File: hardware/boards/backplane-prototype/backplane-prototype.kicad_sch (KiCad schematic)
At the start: 32 parts, among them J1 DC_IN, J2 SLOT_1, J3 SLOT_2, J4 SLOT_3, J5 SLOT_4, J6 SLOT_5, J7 SLOT_6, J8 i2c_busses

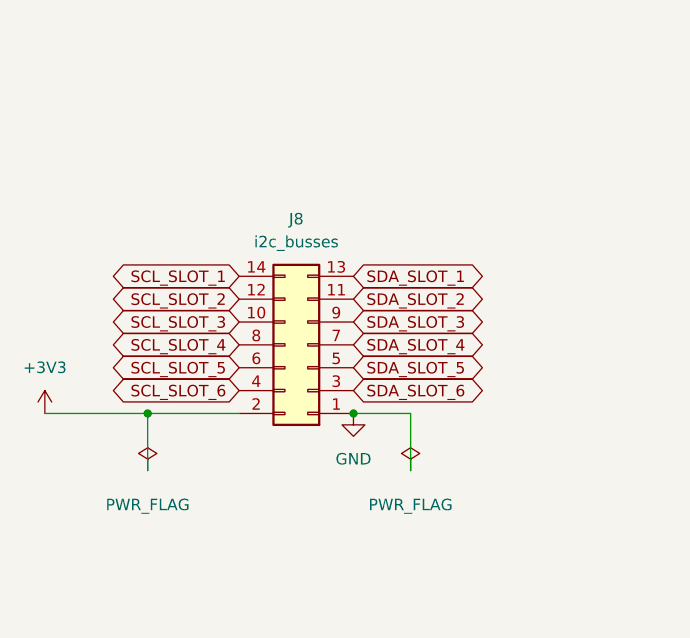
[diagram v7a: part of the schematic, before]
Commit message: feat: connect slot power controls
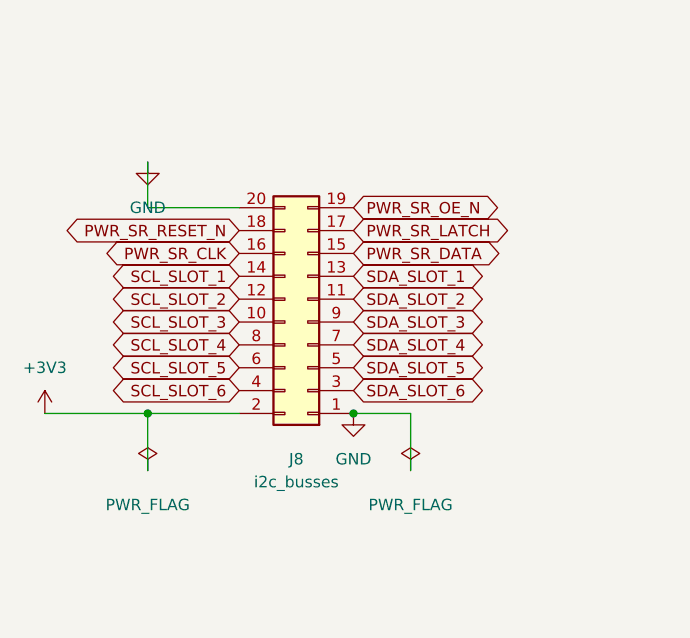
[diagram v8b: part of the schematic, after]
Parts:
- J8: footprint Connector_PinHeader_1.00mm:PinHeader_2x07_P1.00mm_Vertical -> Connector_PinHeader_1.00mm:PinHeader_2x10_P1.00mm_Vertical; symbol Connector_Generic:Conn_02x07_Odd_Even -> Connector_Generic:Conn_02x10_Odd_Even
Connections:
- net GND: now also J8.20 (Pin_20)
- new net PWR_SR_CLK: J8.16 (Pin_16)
- new net PWR_SR_DATA: J8.15 (Pin_15)
- new net PWR_SR_LATCH: J8.17 (Pin_17)
- new net PWR_SR_OE_N: J8.19 (Pin_19)
- new net PWR_SR_RESET_N: J8.18 (Pin_18)
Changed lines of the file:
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@@
 		)
 	)
+	(wire
+		(pts
+			(xy 41.91 140.97) (xy 31.75 140.97)
+		)
+		(stroke
+			(width 0)
+			(type default)
+		)
+	)
+	(wire
+		(pts
+			(xy 31.75 140.97) (xy 31.75 135.89)
+		)
+		(stroke
+			(width 0)
+			(type default)
+		)
+	)
 	(global_label "GND"
 		(shape bidirectional)
@@
 		)
 	)
+	(global_label "PWR_SR_DATA"
+		(shape bidirectional)
+		(at 54.61 146.05 0)
+		(effects
+			(font
+				(size 1.27 1.27)
+			)
+			(justify left)
+		)
+		(property "Intersheetrefs" "${INTERSHEET_REFS}"
+			(at 54.61 146.05 0)
+			(hide yes)
+			(show_name no)
+			(do_not_autoplace no)
+			(effects
+				(font
+					(size 1.27 1.27)
+				)
+			)
+		)
+	)
+	(global_label "PWR_SR_CLK"
+		(shape bidirectional)
+		(at 41.91 146.05 180)
+		(effects
+			(font
+				(size 1.27 1.27)
+			)
+			(justify right)
+		)
+		(property "Intersheetrefs" "${INTERSHEET_REFS}"
+			(at 41.91 146.05 0)
+			(hide yes)
+			(show_name no)
+			(do_not_autoplace no)
+			(effects
+				(font
+					(size 1.27 1.27)
+				)
+			)
+		)
+	)
+	(global_label "PWR_SR_LATCH"
+		(shape bidirectional)
+		(at 54.61 143.51 0)
+		(effects
+			(font
+				(size 1.27 1.27)
+			)
+			(justify left)
+		)
+		(property "Intersheetrefs" "${INTERSHEET_REFS}"
+			(at 54.61 143.51 0)
+			(hide yes)
+			(show_name no)
+			(do_not_autoplace no)
+			(effects
+				(font
+					(size 1.27 1.27)
+				)
+			)
+		)
+	)
+	(global_label "PWR_SR_RESET_N"
+		(shape bidirectional)
+		(at 41.91 143.51 180)
+		(effects
+			(font
+				(size 1.27 1.27)
+			)
+			(justify right)
+		)
+		(property "Intersheetrefs" "${INTERSHEET_REFS}"
+			(at 41.91 143.51 0)
+			(hide yes)
+			(show_name no)
+			(do_not_autoplace no)
+			(effects
+				(font
+					(size 1.27 1.27)
+				)
+			)
+		)
+	)
+	(global_label "PWR_SR_OE_N"
+		(shape bidirectional)
+		(at 54.61 140.97 0)
+		(effects
+			(font
+				(size 1.27 1.27)
+			)
+			(justify left)
+		)
+		(property "Intersheetrefs" "${INTERSHEET_REFS}"
+			(at 54.61 140.97 0)
+			(hide yes)
+			(show_name no)
+			(do_not_autoplace no)
+			(effects
+				(font
+					(size 1.27 1.27)
+				)
+			)
+		)
+	)
 	(symbol
 		(lib_id "power:GND")
@@
 	)
 	(symbol
-		(lib_id "Connector_Generic:Conn_02x07_Odd_Even")
-		(at 49.53 156.21 180)
+		(lib_id "power:GND")
+		(at 31.75 135.89 0)
+		(unit 1)
+		(body_style 1)
+		(exclude_from_sim no)
+		(in_bom yes)
+		(on_board yes)
+		(in_pos_files yes)
+		(dnp no)
+		(fields_autoplaced yes)
+		(property "Reference" "#PWR0100"
+			(at 31.75 142.24 0)
+			(hide yes)
+			(show_name no)
+			(do_not_autoplace no)
+			(effects
+				(font
+					(size 1.27 1.27)
+				)
+			)
+		)
+		(property "Value" "GND"
+			(at 31.75 140.97 0)
+			(show_name no)
+			(do_not_autoplace no)
+			(effects
+				(font
+					(size 1.27 1.27)
+				)
+			)
+		)
+		(property "Footprint" ""
+			(at 31.75 135.89 0)
+			(hide yes)
+			(show_name no)
+			(do_not_autoplace no)
+			(effects
+				(font
+					(size 1.27 1.27)
+				)
+			)
+		)
+		(property "Datasheet" ""
+			(at 31.75 135.89 0)
+			(hide yes)
+			(show_name no)
+			(do_not_autoplace no)
+			(effects
+				(font
+					(size 1.27 1.27)
+				)
+			)
+		)
+		(property "Description" "Power symbol creates a global label with name \"GND\" , ground"
+			(at 31.75 135.89 0)
+			(hide yes)
+			(show_name no)
+			(do_not_autoplace no)
+			(effects
+				(font
+					(size 1.27 1.27)
+				)
+			)
+		)
+		(pin "1"
+		)
+		(instances
+			(project "backplane-prototype"
+				(path "/348cc909-6345-4013-9bef-98714057a65b"
+					(reference "#PWR0100")
+					(unit 1)
+				)
+			)
+		)
+	)
+	(symbol
+		(lib_id "Connector_Generic:Conn_02x10_Odd_Even")
+		(at 49.53 153.67 180)
 		(unit 1)
 		(body_style 1)
@@
 		(fields_autoplaced yes)
 		(property "Reference" "J8"
-			(at 48.26 142.24 0)
+			(at 48.26 168.91 0)
 			(show_name no)
 			(do_not_autoplace no)
@@
 		)
 		(property "Value" "i2c_busses"
-			(at 48.26 144.78 0)
+			(at 48.26 171.45 0)
 			(show_name no)
 			(do_not_autoplace no)
@@
 			)
 		)
-		(property "Footprint" "Connector_PinHeader_1.00mm:PinHeader_2x07_P1.00mm_Vertical"
-			(at 49.53 156.21 0)
+		(property "Footprint" "Connector_PinHeader_1.00mm:PinHeader_2x10_P1.00mm_Vertical"
+			(at 49.53 153.67 0)
 			(hide yes)
 			(show_name no)
@@
 		)
 		(property "Datasheet" ""
-			(at 49.53 156.21 0)
+			(at 49.53 153.67 0)
 			(hide yes)
 			(show_name no)
@@
 			)
 		)
-		(property "Description" "Generic connector, double row, 02x07, odd/even pin numbering scheme (row 1 odd numbers, row 2 even numbers), script generated (kicad-library-utils/schlib/autogen/connector/)"
-			(at 49.53 156.21 0)
+		(property "Description" "Generic connector, double row, 02x10, odd/even pin numbering scheme (row 1 odd numbers, row 2 even numbers), script generated (kicad-library-utils/schlib/autogen/connector/)"
+			(at 49.53 153.67 0)
 			(hide yes)
 			(show_name no)
@@
 		(pin "14"
 		)
+		(pin "15"
+		)
+		(pin "16"
+		)
+		(pin "17"
+		)
+		(pin "18"
+		)
+		(pin "19"
+		)
+		(pin "20"
+		)
 		(instances
